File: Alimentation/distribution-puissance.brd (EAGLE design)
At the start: 93.7 x 48.2 mm, 18 parts

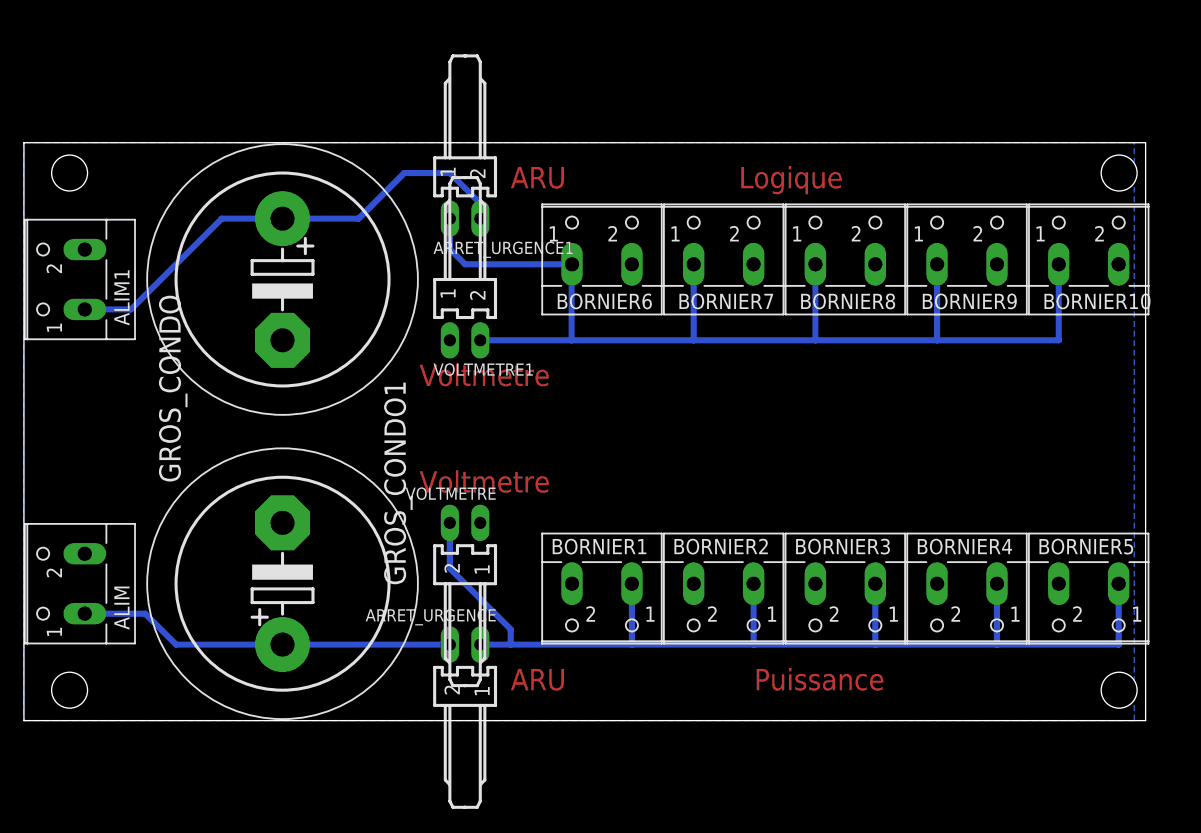
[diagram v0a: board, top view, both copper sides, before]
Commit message: utilisation de bornier pour les ARU + plus grosses pistes dans le routage + gerber files
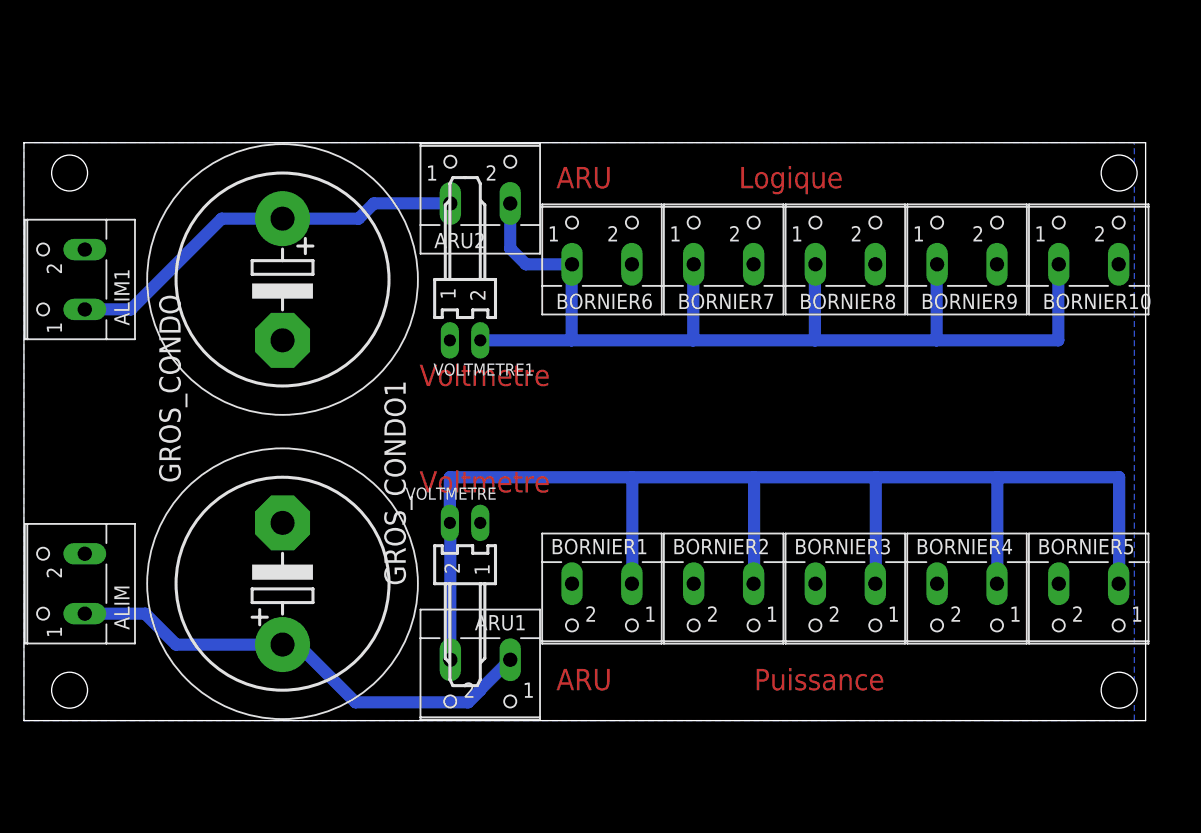
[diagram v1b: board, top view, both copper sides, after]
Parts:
- removed ARRET_URGENCE, ARRET_URGENCE1: 22-05-7028-02, con-molex:7395-02
- added ARU1, ARU2: 19V, con-wago-500:W237-102
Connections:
- net N$1: now also ARU1.2; no longer ARRET_URGENCE.1
- net N$2: now also ARU2.2; no longer ARRET_URGENCE1.1
- net N$3: now also ARU1.1; no longer ARRET_URGENCE.2
- net N$4: now also ARU2.1; no longer ARRET_URGENCE1.2
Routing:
- net N$1: track 91.2 -> 115.7 mm
- net N$3: track 31.5 -> 40.1 mm
- net N$4: track 40.1 -> 34.2 mm
- net N$2: track 93.4 -> 89.6 mm

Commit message: carte puissance v2
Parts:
- removed ALIM, ALIM1, ARU1, ARU2, BORNIER1, BORNIER10, BORNIER2, BORNIER3, BORNIER4, BORNIER5, BORNIER6, BORNIER7, BORNIER8, BORNIER9: 19V, con-wago-500:W237-102
- added ALIM-LOGIQUE, ARU-LOGIQUE, INTERUPTEUR-LOGIQUE: 5V, con-wago-500:W237-102
- added ALIM-PUISSANCE, ARU-PUISSANCE, INTERUPTEUR-PUISSANCE, PUISSANCE1, PUISSANCE2, PUISSANCE3, PUISSANCE4, PUISSANCE5: 19V, con-wago-500:W237-102
- added LOGIQUE1, LOGIQUE2, LOGIQUE3, LOGIQUE4, LOGIQUE5: 22-05-7028-02, con-molex:7395-02
- moved VOLTMETRE 8.52 mm to (44.5, 20.3)
- moved VOLTMETRE1 8.03 mm to (44.5, 29.2)
- moved GROS_CONDO1 1.27 mm to (21.6, 35.6)
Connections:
- new net N$5: ARU-PUISSANCE.2, INTERUPTEUR-PUISSANCE.1
- new net N$6: ARU-LOGIQUE.2, INTERUPTEUR-LOGIQUE.1
- net GND: now also ALIM-LOGIQUE.2, ALIM-PUISSANCE.2, LOGIQUE1.1, LOGIQUE2.1, LOGIQUE3.1, LOGIQUE4.1, LOGIQUE5.1, PUISSANCE1.2, PUISSANCE2.2, PUISSANCE3.2, PUISSANCE4.2, PUISSANCE5.2; no longer ALIM.2, ALIM1.2, BORNIER1.2, BORNIER10.2, BORNIER2.2, BORNIER3.2, BORNIER4.2, BORNIER5.2, BORNIER6.2, BORNIER7.2, BORNIER8.2, BORNIER9.2
- net N$1: now also INTERUPTEUR-PUISSANCE.2, PUISSANCE1.1, PUISSANCE2.1, PUISSANCE3.1, PUISSANCE4.1, PUISSANCE5.1; no longer ARU1.2, BORNIER1.1, BORNIER2.1, BORNIER3.1, BORNIER4.1, BORNIER5.1
- net N$2: now also INTERUPTEUR-LOGIQUE.2, LOGIQUE1.2, LOGIQUE2.2, LOGIQUE3.2, LOGIQUE4.2, LOGIQUE5.2; no longer ARU2.2, BORNIER10.1, BORNIER6.1, BORNIER7.1, BORNIER8.1, BORNIER9.1
- net N$3: now also ALIM-PUISSANCE.1, ARU-PUISSANCE.1; no longer ALIM.1, ARU1.1
- net N$4: now also ALIM-LOGIQUE.1, ARU-LOGIQUE.1; no longer ALIM1.1, ARU2.1
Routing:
- net N$2: track 89.6 -> 62.3 mm
- net N$5: track 0.00 -> 23.2 mm
- net N$1: track 115.7 -> 127.9 mm
- net N$6: track 0.00 -> 5.16 mm
- net N$3: track 40.1 -> 44.8 mm
- net N$4: track 34.2 -> 37.6 mm
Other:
- board size 93.7 x 48.2 mm -> 84.8 x 48.2 mm
- board text removed: "ARU"
